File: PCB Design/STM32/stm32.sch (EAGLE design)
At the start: 68 parts, among them IC1 NCP1117ST50T3G, Q1 ABM3B-8.000MHZ-10-1UT, T1 SFH303, T2 SFH303, T3 SFH303, T4 SFH303, T5 BC847, T6 BC847, T7 BC847, T8 BC847, U1 STM32F103RET6, U2 MCP1700T-3302E/TT, U3 MCP1700T-3302E/TT, U4 MPU-6050, U5 TB6612FNG, X1 22-23-2031

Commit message: minor update
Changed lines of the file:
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@@
 <parts>
 <part name="Q1" library="SparkFun-FreqCtrl" deviceset="CRYSTAL-GROUNDED" device="" value="ABM3B-8.000MHZ-10-1UT"/>
-<part name="GND10" library="SparkFun" deviceset="GND" device=""/>
+<part name="GND10" library="SparkFun-Aesthetics" deviceset="GND" device=""/>
 <part name="C12" library="SparkFun-Capacitors" deviceset="CAP" device="0805" value="10pF"/>
 <part name="C13" library="SparkFun-Capacitors" deviceset="CAP" device="0805" value="10pF"/>
-<part name="P+1" library="SparkFun" deviceset="VCC" device=""/>
-<part name="GND1" library="SparkFun" deviceset="GND" device=""/>
-<part name="P+3" library="SparkFun" deviceset="VCC" device=""/>
-<part name="GND7" library="SparkFun" deviceset="GND" device=""/>
-<part name="GND9" library="SparkFun" deviceset="GND" device=""/>
-<part name="VDD3" library="supply1" deviceset="VDD" device="" value="VDDA"/>
-<part name="VDD1" library="supply1" deviceset="VDD" device="" value="VDDA"/>
-<part name="GND8" library="SparkFun" deviceset="GND" device=""/>
-<part name="GND2" library="SparkFun" deviceset="GND" device=""/>
+<part name="P+1" library="SparkFun-Aesthetics" deviceset="VCC" device=""/>
+<part name="GND1" library="SparkFun-Aesthetics" deviceset="GND" device=""/>
+<part name="P+3" library="SparkFun-Aesthetics" deviceset="VCC" device=""/>
+<part name="GND7" library="SparkFun-Aesthetics" deviceset="GND" device=""/>
+<part name="GND9" library="SparkFun-Aesthetics" deviceset="GND" device=""/>
+<part name="VDD3" library="SparkFun-Aesthetics" deviceset="VDD" device="" value="VDDA"/>
+<part name="VDD1" library="SparkFun-Aesthetics" deviceset="VDD" device="" value="VDDA"/>
+<part name="GND8" library="SparkFun-Aesthetics" deviceset="GND" device=""/>
+<part name="GND2" library="SparkFun-Aesthetics" deviceset="GND" device=""/>
 <part name="U4" library="SparkFun-Sensors" deviceset="MPU-6000" device="QFN-24" value="MPU-6050"/>
 <part name="SUPPLY6" library="SparkFun-Aesthetics" deviceset="VCC" device=""/>
@@
 <part name="GND26" library="SparkFun-Aesthetics" deviceset="GND" device=""/>
 <part name="U1" library="ST Microelctronics_By_element14_Batch_1" deviceset="STM32F103RET6" device=""/>
-<part name="P+2" library="SparkFun" deviceset="VCC" device=""/>
-<part name="VDD2" library="supply1" deviceset="VDD" device="" value="VDDA"/>
-<part name="GND5" library="SparkFun" deviceset="GND" device=""/>
+<part name="P+2" library="SparkFun-Aesthetics" deviceset="VCC" device=""/>
+<part name="VDD2" library="SparkFun-Aesthetics" deviceset="VDD" device="" value="VDDA"/>
+<part name="GND5" library="SparkFun-Aesthetics" deviceset="GND" device=""/>
 <part name="IC1" library="linear" deviceset="MC33269ST*" device="" technology="-3.3T3" value="NCP1117ST50T3G"/>
 <part name="SUPPLY16" library="SparkFun-Aesthetics" deviceset="5V" device=""/>
@@
 <part name="C11" library="SparkFun-Capacitors" deviceset="CAP" device="0805" value="10uF"/>
 <part name="C9" library="SparkFun-Capacitors" deviceset="CAP" device="0805" value="10uF"/>
-<part name="GND38" library="SparkFun" deviceset="GND" device=""/>
+<part name="GND38" library="SparkFun-Aesthetics" deviceset="GND" device=""/>
 <part name="SUPPLY21" library="SparkFun-Aesthetics" deviceset="5V" device=""/>
 <part name="C22" library="SparkFun-Capacitors" deviceset="CAP" device="0805" value="10uF"/>
@@
 <attribute name="VALUE" x="241.3" y="248.92" size="1.778" layer="96"/>
 </instance>
-<instance part="P+1" gate="1" x="99.06" y="226.06"/>
+<instance part="P+1" gate="G$1" x="99.06" y="226.06"/>
 <instance part="GND1" gate="1" x="99.06" y="205.74" rot="MR0"/>
-<instance part="P+3" gate="1" x="241.3" y="86.36" smashed="yes">
+<instance part="P+3" gate="G$1" x="241.3" y="86.36" smashed="yes">
 <attribute name="VALUE" x="242.824" y="87.376" size="1.778" layer="96"/>
 </instance>
 <instance part="GND7" gate="1" x="177.8" y="68.58"/>
 <instance part="GND9" gate="1" x="241.3" y="66.04"/>
-<instance part="VDD3" gate="G$1" x="241.3" y="116.84" smashed="yes">
+<instance part="VDD3" gate="VDD" x="241.3" y="116.84" smashed="yes">
 <attribute name="VALUE" x="243.84" y="114.3" size="1.778" layer="96"/>
 </instance>
-<instance part="VDD1" gate="G$1" x="104.14" y="264.16" smashed="yes">
+<instance part="VDD1" gate="VDD" x="104.14" y="264.16" smashed="yes">
 <attribute name="VALUE" x="101.6" y="266.7" size="1.778" layer="96"/>
 </instance>
@@
 <instance part="GND26" gate="1" x="429.26" y="205.74"/>
 <instance part="U1" gate="A" x="193.04" y="205.74"/>
-<instance part="P+2" gate="1" x="154.94" y="254"/>
-<instance part="VDD2" gate="G$1" x="154.94" y="266.7" smashed="yes">
+<instance part="P+2" gate="G$1" x="154.94" y="254"/>
+<instance part="VDD2" gate="VDD" x="154.94" y="266.7" smashed="yes">
 <attribute name="VALUE" x="152.4" y="269.24" size="1.778" layer="96"/>
 </instance>
@@
 <pinref part="C3" gate="G$1" pin="1"/>
 <pinref part="C4" gate="G$1" pin="1"/>
-<pinref part="P+1" gate="1" pin="VCC"/>
+<pinref part="P+1" gate="G$1" pin="VCC"/>
 <pinref part="C5" gate="G$1" pin="1"/>
 <pinref part="C6" gate="G$1" pin="1"/>
@@
 <segment>
 <wire x1="241.3" y1="81.28" x2="241.3" y2="83.82" width="0.1524" layer="91"/>
-<pinref part="P+3" gate="1" pin="VCC"/>
+<pinref part="P+3" gate="G$1" pin="VCC"/>
 <pinref part="U3" gate="A" pin="VOUT"/>
 <wire x1="241.3" y1="83.82" x2="241.3" y2="86.36" width="0.1524" layer="91"/>
@@
 <wire x1="162.56" y1="256.54" x2="160.02" y2="256.54" width="0.1524" layer="91"/>
 <wire x1="160.02" y1="251.46" x2="154.94" y2="251.46" width="0.1524" layer="91"/>
-<pinref part="P+2" gate="1" pin="VCC"/>
+<pinref part="P+2" gate="G$1" pin="VCC"/>
 <wire x1="154.94" y1="251.46" x2="154.94" y2="254" width="0.1524" layer="91"/>
 <junction x="160.02" y="256.54"/>
@@
 <wire x1="228.6" y1="111.76" x2="241.3" y2="111.76" width="0.1524" layer="91"/>
 <wire x1="241.3" y1="111.76" x2="241.3" y2="109.22" width="0.1524" layer="91"/>
-<wire x1="241.3" y1="111.76" x2="241.3" y2="114.3" width="0.1524" layer="91"/>
+<wire x1="241.3" y1="111.76" x2="241.3" y2="116.84" width="0.1524" layer="91"/>
 <junction x="241.3" y="111.76"/>
-<pinref part="VDD3" gate="G$1" pin="VDD"/>
+<pinref part="VDD3" gate="VDD" pin="VDD"/>
 <pinref part="U2" gate="A" pin="VOUT"/>
 <pinref part="C10" gate="G$1" pin="1"/>
@@
 <pinref part="U1" gate="A" pin="VDDA"/>
 <wire x1="162.56" y1="261.62" x2="154.94" y2="261.62" width="0.1524" layer="91"/>
-<pinref part="VDD2" gate="G$1" pin="VDD"/>
-<wire x1="154.94" y1="261.62" x2="154.94" y2="264.16" width="0.1524" layer="91"/>
+<pinref part="VDD2" gate="VDD" pin="VDD"/>
+<wire x1="154.94" y1="261.62" x2="154.94" y2="266.7" width="0.1524" layer="91"/>
 </segment>
 <segment>
@@
 <wire x1="104.14" y1="259.08" x2="99.06" y2="259.08" width="0.1524" layer="91"/>
 <wire x1="99.06" y1="259.08" x2="99.06" y2="256.54" width="0.1524" layer="91"/>
-<pinref part="VDD1" gate="G$1" pin="VDD"/>
-<wire x1="104.14" y1="259.08" x2="104.14" y2="261.62" width="0.1524" layer="91"/>
+<pinref part="VDD1" gate="VDD" pin="VDD"/>
+<wire x1="104.14" y1="259.08" x2="104.14" y2="264.16" width="0.1524" layer="91"/>
 <junction x="104.14" y="259.08"/>
 </segment>

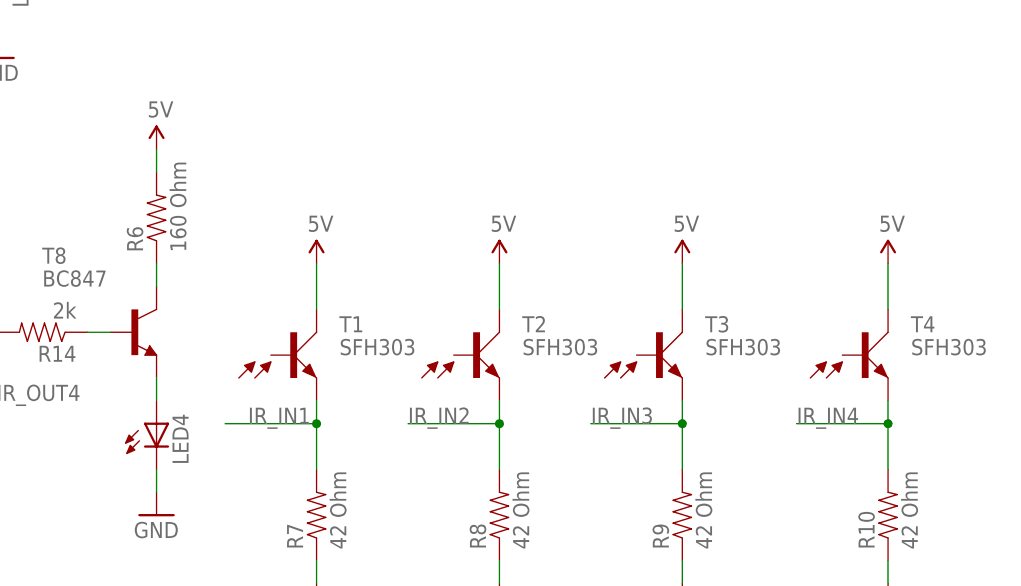
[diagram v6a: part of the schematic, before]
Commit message: changed to new phototransistors
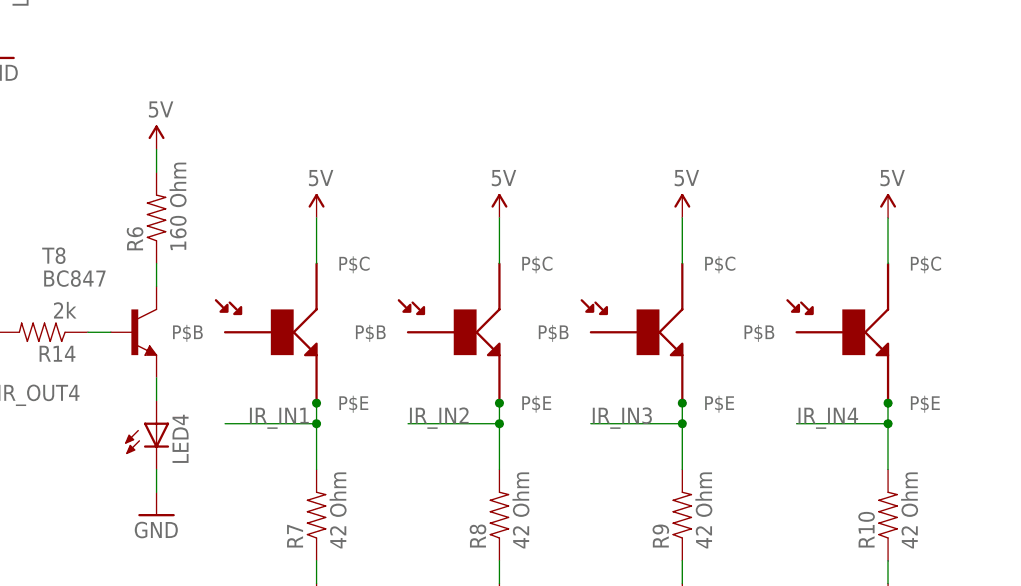
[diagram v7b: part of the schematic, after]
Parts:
- removed T1, T2, T3, T4: SFH303, opto-trans-siemens:SFH303
- added U$2, U$3, U$4, U$5: PHTRST, phototransistor:PHTRST
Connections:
- net 5V: now also U$2.P$C, U$3.P$C, U$4.P$C, U$5.P$C; no longer T1.C, T2.C, T3.C, T4.C
- net IR_IN1: now also U$2.P$E; no longer T1.E
- net IR_IN2: now also U$3.P$E; no longer T2.E
- net IR_IN3: now also U$4.P$E; no longer T3.E
- net IR_IN4: now also U$5.P$E; no longer T4.E
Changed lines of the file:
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@@
 <part name="U2" library="Microchip_By_element14_Batch_1" deviceset="MCP1700T-3302E/TT" device=""/>
 <part name="U3" library="Microchip_By_element14_Batch_1" deviceset="MCP1700T-3302E/TT" device=""/>
-<part name="T2" library="opto-trans-siemens" deviceset="SFH303" device=""/>
-<part name="T3" library="opto-trans-siemens" deviceset="SFH303" device=""/>
-<part name="T4" library="opto-trans-siemens" deviceset="SFH303" device=""/>
-<part name="T1" library="opto-trans-siemens" deviceset="SFH303" device=""/>
 <part name="LED1" library="led" deviceset="LED" device="5MM"/>
 <part name="LED2" library="led" deviceset="LED" device="5MM"/>
@@
 <part name="T7" library="transistor" deviceset="BC847" device=""/>
 <part name="T8" library="transistor" deviceset="BC847" device=""/>
+<part name="U$2" library="phototransistor" deviceset="PHTRST" device=""/>
+<part name="U$3" library="phototransistor" deviceset="PHTRST" device=""/>
+<part name="U$4" library="phototransistor" deviceset="PHTRST" device=""/>
+<part name="U$5" library="phototransistor" deviceset="PHTRST" device=""/>
 </parts>
 <sheets>
@@
 <instance part="U2" gate="A" x="210.82" y="111.76"/>
 <instance part="U3" gate="A" x="210.82" y="83.82"/>
-<instance part="T2" gate="G$1" x="383.54" y="233.68"/>
-<instance part="T3" gate="G$1" x="403.86" y="233.68"/>
-<instance part="T4" gate="G$1" x="426.72" y="233.68"/>
-<instance part="T1" gate="G$1" x="363.22" y="233.68"/>
 <instance part="LED1" gate="G$1" x="276.86" y="226.06"/>
 <instance part="LED2" gate="G$1" x="299.72" y="226.06"/>
@@
 <instance part="SUPPLY7" gate="G$1" x="322.58" y="256.54"/>
 <instance part="SUPPLY8" gate="G$1" x="347.98" y="256.54"/>
-<instance part="SUPPLY9" gate="G$1" x="365.76" y="243.84"/>
-<instance part="SUPPLY10" gate="G$1" x="386.08" y="243.84"/>
-<instance part="SUPPLY12" gate="G$1" x="406.4" y="243.84"/>
-<instance part="SUPPLY13" gate="G$1" x="429.26" y="243.84"/>
+<instance part="SUPPLY9" gate="G$1" x="365.76" y="248.92"/>
+<instance part="SUPPLY10" gate="G$1" x="386.08" y="248.92"/>
+<instance part="SUPPLY12" gate="G$1" x="406.4" y="248.92"/>
+<instance part="SUPPLY13" gate="G$1" x="429.26" y="248.92"/>
 <instance part="GND27" gate="1" x="109.22" y="83.82"/>
 <instance part="GND28" gate="1" x="127" y="83.82"/>
@@
 <instance part="T7" gate="G$1" x="320.04" y="236.22"/>
 <instance part="T8" gate="G$1" x="345.44" y="236.22"/>
+<instance part="U$2" gate="G$1" x="363.22" y="236.22"/>
+<instance part="U$3" gate="G$1" x="383.54" y="236.22"/>
+<instance part="U$4" gate="G$1" x="403.86" y="236.22"/>
+<instance part="U$5" gate="G$1" x="426.72" y="236.22"/>
 </instances>
 <busses>
@@
 </segment>
 <segment>
-<pinref part="T1" gate="G$1" pin="E"/>
 <pinref part="R7" gate="G$1" pin="2"/>
 <wire x1="365.76" y1="220.98" x2="365.76" y2="226.06" width="0.1524" layer="91"/>
-<wire x1="365.76" y1="226.06" x2="365.76" y2="228.6" width="0.1524" layer="91"/>
+<wire x1="365.76" y1="226.06" x2="365.76" y2="228.346" width="0.1524" layer="91"/>
+<wire x1="365.76" y1="228.346" x2="365.76" y2="228.6" width="0.1524" layer="91"/>
 <wire x1="365.76" y1="226.06" x2="355.6" y2="226.06" width="0.1524" layer="91"/>
 <label x="358.14" y="226.06" size="1.778" layer="95"/>
 <junction x="365.76" y="226.06"/>
+<pinref part="U$2" gate="G$1" pin="P$E"/>
+<junction x="365.76" y="228.346"/>
 </segment>
 </net>
@@
 </segment>
 <segment>
-<pinref part="T2" gate="G$1" pin="E"/>
 <pinref part="R8" gate="G$1" pin="2"/>
 <wire x1="386.08" y1="220.98" x2="386.08" y2="226.06" width="0.1524" layer="91"/>
-<wire x1="386.08" y1="226.06" x2="386.08" y2="228.6" width="0.1524" layer="91"/>
+<wire x1="386.08" y1="226.06" x2="386.08" y2="228.346" width="0.1524" layer="91"/>
+<wire x1="386.08" y1="228.346" x2="386.08" y2="228.6" width="0.1524" layer="91"/>
 <wire x1="375.92" y1="226.06" x2="386.08" y2="226.06" width="0.1524" layer="91"/>
 <label x="375.92" y="226.06" size="1.778" layer="95"/>
 <junction x="386.08" y="226.06"/>
+<pinref part="U$3" gate="G$1" pin="P$E"/>
+<junction x="386.08" y="228.346"/>
 </segment>
 </net>
@@
 </segment>
 <segment>
-<pinref part="T3" gate="G$1" pin="E"/>
 <pinref part="R9" gate="G$1" pin="2"/>
 <wire x1="406.4" y1="220.98" x2="406.4" y2="226.06" width="0.1524" layer="91"/>
-<wire x1="406.4" y1="226.06" x2="406.4" y2="228.6" width="0.1524" layer="91"/>
+<wire x1="406.4" y1="226.06" x2="406.4" y2="228.346" width="0.1524" layer="91"/>
+<wire x1="406.4" y1="228.346" x2="406.4" y2="228.6" width="0.1524" layer="91"/>
 <wire x1="396.24" y1="226.06" x2="406.4" y2="226.06" width="0.1524" layer="91"/>
 <label x="396.24" y="226.06" size="1.778" layer="95"/>
 <junction x="406.4" y="226.06"/>
+<pinref part="U$4" gate="G$1" pin="P$E"/>
+<junction x="406.4" y="228.346"/>
 </segment>
 </net>
@@
 </segment>
 <segment>
-<pinref part="T4" gate="G$1" pin="E"/>
 <pinref part="R10" gate="G$1" pin="2"/>
 <wire x1="429.26" y1="220.98" x2="429.26" y2="226.06" width="0.1524" layer="91"/>
-<wire x1="429.26" y1="226.06" x2="429.26" y2="228.6" width="0.1524" layer="91"/>
+<wire x1="429.26" y1="226.06" x2="429.26" y2="228.346" width="0.1524" layer="91"/>
+<wire x1="429.26" y1="228.346" x2="429.26" y2="228.6" width="0.1524" layer="91"/>
 <wire x1="419.1" y1="226.06" x2="429.26" y2="226.06" width="0.1524" layer="91"/>
 <label x="419.1" y="226.06" size="1.778" layer="95"/>
 <junction x="429.26" y="226.06"/>
+<pinref part="U$5" gate="G$1" pin="P$E"/>
+<junction x="429.26" y="228.346"/>
 </segment>
 </net>
@@
 </segment>
 <segment>
-<pinref part="T1" gate="G$1" pin="C"/>
-<wire x1="365.76" y1="243.84" x2="365.76" y2="238.76" width="0.1524" layer="91"/>
+<wire x1="365.76" y1="248.92" x2="365.76" y2="243.84" width="0.1524" layer="91"/>
 <pinref part="SUPPLY9" gate="G$1" pin="5V"/>
-</segment>
-<segment>
-<pinref part="T2" gate="G$1" pin="C"/>
-<wire x1="386.08" y1="243.84" x2="386.08" y2="238.76" width="0.1524" layer="91"/>
+<pinref part="U$2" gate="G$1" pin="P$C"/>
+</segment>
+<segment>
+<wire x1="386.08" y1="248.92" x2="386.08" y2="243.84" width="0.1524" layer="91"/>
 <pinref part="SUPPLY10" gate="G$1" pin="5V"/>
-</segment>
-<segment>
-<pinref part="T3" gate="G$1" pin="C"/>
-<wire x1="406.4" y1="243.84" x2="406.4" y2="238.76" width="0.1524" layer="91"/>
+<pinref part="U$3" gate="G$1" pin="P$C"/>
+</segment>
+<segment>
+<wire x1="406.4" y1="248.92" x2="406.4" y2="243.84" width="0.1524" layer="91"/>
 <pinref part="SUPPLY12" gate="G$1" pin="5V"/>
-</segment>
-<segment>
-<pinref part="T4" gate="G$1" pin="C"/>
-<wire x1="429.26" y1="243.84" x2="429.26" y2="238.76" width="0.1524" layer="91"/>
+<pinref part="U$4" gate="G$1" pin="P$C"/>
+</segment>
+<segment>
+<wire x1="429.26" y1="248.92" x2="429.26" y2="243.84" width="0.1524" layer="91"/>
 <pinref part="SUPPLY13" gate="G$1" pin="5V"/>
-</segment>
-<segment>
+<pinref part="U$5" gate="G$1" pin="P$C"/>
+</segment>
+<segment>
